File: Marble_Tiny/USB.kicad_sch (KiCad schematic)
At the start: 40 parts, among them J2 USB_C_Receptacle_USB2.0_16P, Q2 XTAL_12MHZ_TXC_7A-12.000MAAJ-T, U21 FT2232HQ, U22 93C46B-I_SN, U8 TLV62565DBV

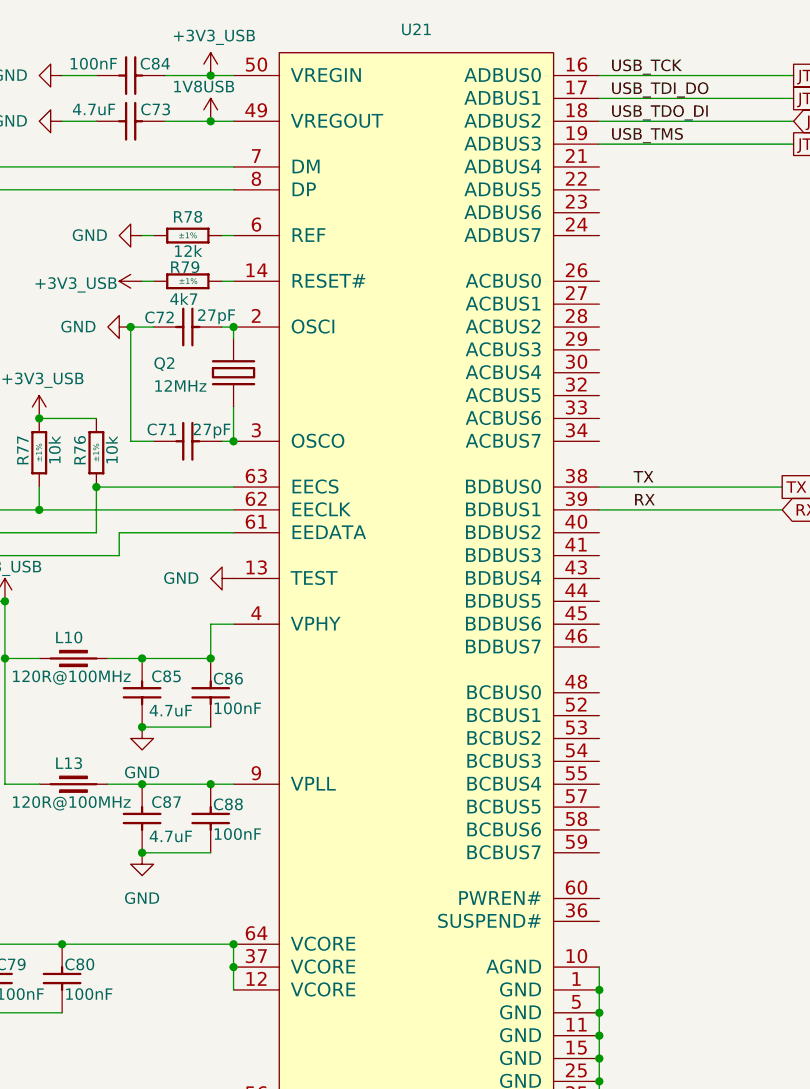
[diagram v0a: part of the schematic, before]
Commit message: fixed ERCs; added test points; added WP switch
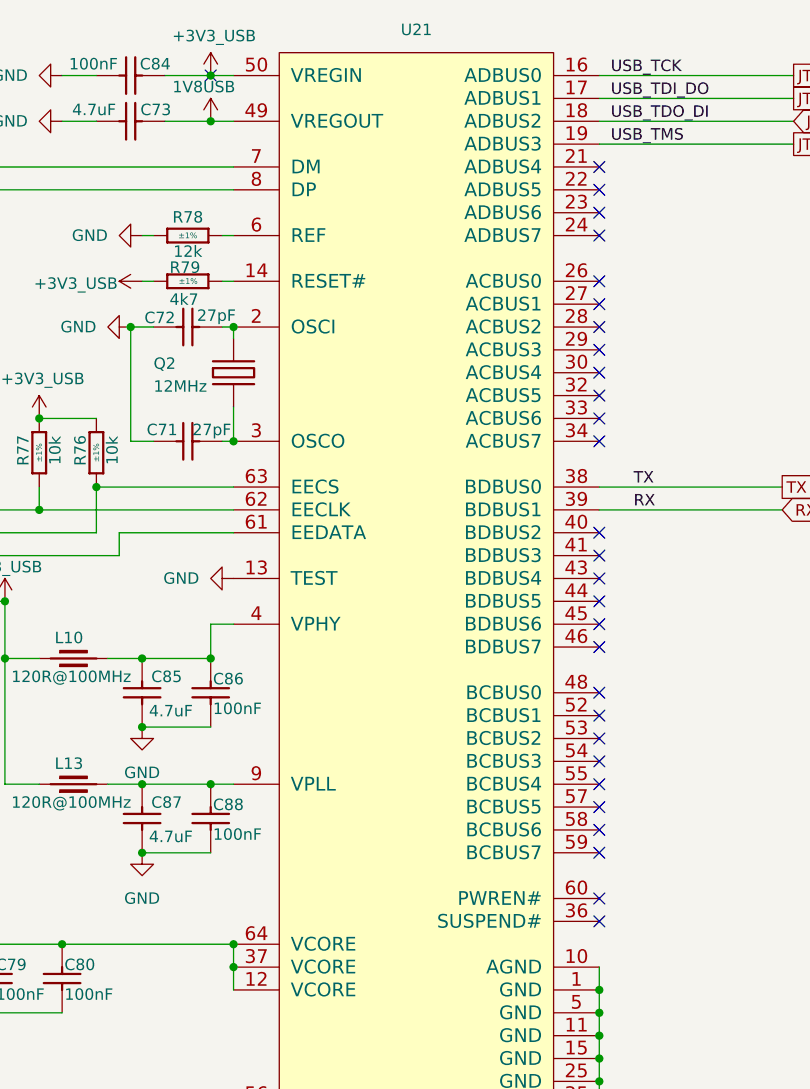
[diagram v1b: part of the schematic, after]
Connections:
- no-connect marks 4 -> 33
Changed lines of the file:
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@@
+	)
+	(no_connect
+		(at 222.25 102.87)
+	)
+	(no_connect
+		(at 222.25 54.61)
+	)
+	(no_connect
+		(at 222.25 82.55)
+	)
+	(no_connect
+		(at 222.25 120.65)
+	)
+	(no_connect
+		(at 222.25 87.63)
+	)
+	(no_connect
+		(at 222.25 105.41)
+	)
+	(no_connect
+		(at 222.25 113.03)
+	)
+	(no_connect
+		(at 179.07 29.21)
+	)
+	(no_connect
+		(at 222.25 44.45)
+	)
+	(no_connect
+		(at 222.25 107.95)
+	)
+	(no_connect
+		(at 222.25 110.49)
+	)
+	(no_connect
+		(at 222.25 52.07)
+	)
+	(no_connect
+		(at 222.25 67.31)
+	)
+	(no_connect
+		(at 222.25 46.99)
+	)
+	(no_connect
+		(at 222.25 92.71)
+	)
+	(no_connect
+		(at 222.25 41.91)
+	)
+	(no_connect
+		(at 222.25 39.37)
 	)
 	(no_connect
@@
 	)
 	(no_connect
+		(at 222.25 123.19)
+	)
+	(no_connect
+		(at 222.25 80.01)
+	)
+	(no_connect
+		(at 222.25 62.23)
+	)
+	(no_connect
 		(at 64.77 63.5)
+	)
+	(no_connect
+		(at 222.25 100.33)
 	)
 	(no_connect
@@
 	)
 	(no_connect
+		(at 222.25 115.57)
+	)
+	(no_connect
+		(at 222.25 85.09)
+	)
+	(no_connect
+		(at 222.25 69.85)
+	)
+	(no_connect
+		(at 222.25 90.17)
+	)
+	(no_connect
+		(at 222.25 64.77)
+	)
+	(no_connect
 		(at 148.59 82.55)
 	)
+	(no_connect
+		(at 222.25 59.69)
+	)
+	(no_connect
+		(at 222.25 57.15)
+	)
+	(no_connect
+		(at 222.25 97.79)
+	)
 	(wire

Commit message: fixed issue with PMODs; added board name and revision; fixed polygons issue
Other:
- company: (none) -> ${name}
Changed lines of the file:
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@@
 	(generator_version "9.0")
 	(paper "A4")
+	(title_block
+		(date "2025-04-18")
+		(rev "${rev}")
+		(company "${name}")
+		(comment 1 "${author}")
+	)
 	(junction
 		(at 147.32 125.73)
